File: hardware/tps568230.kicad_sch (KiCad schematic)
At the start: 24 parts, among them U1 TPS568230, U4 LD39050PU33R

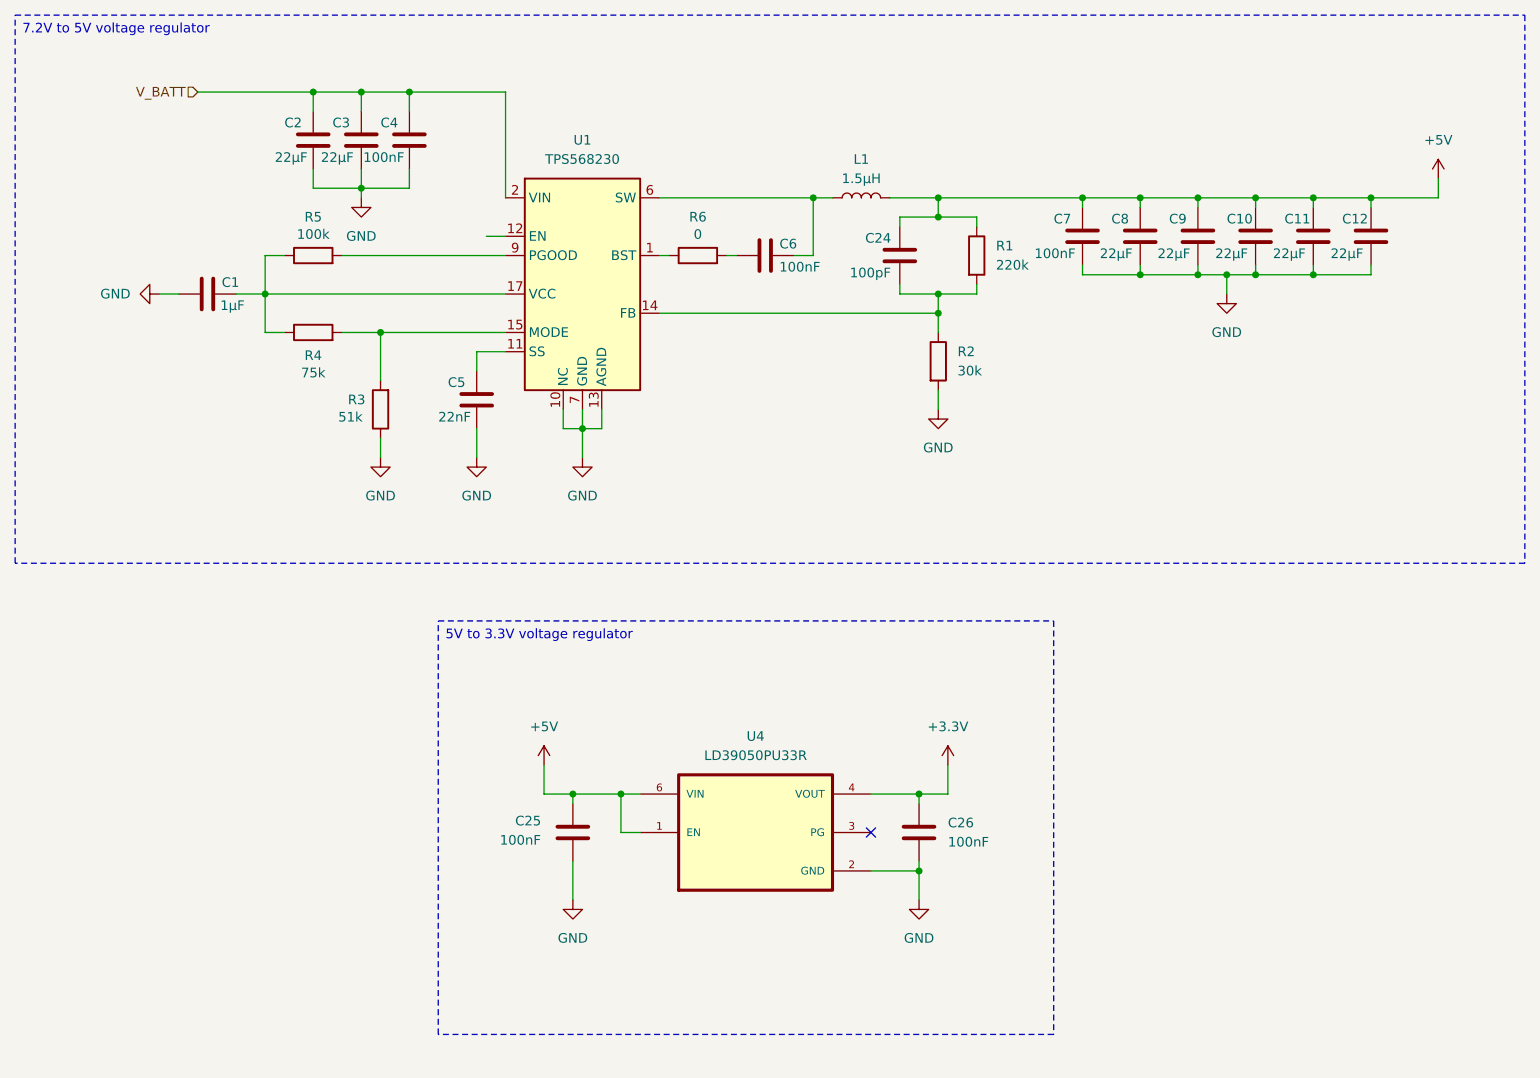
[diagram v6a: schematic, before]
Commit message: Adding voltage divider to EN
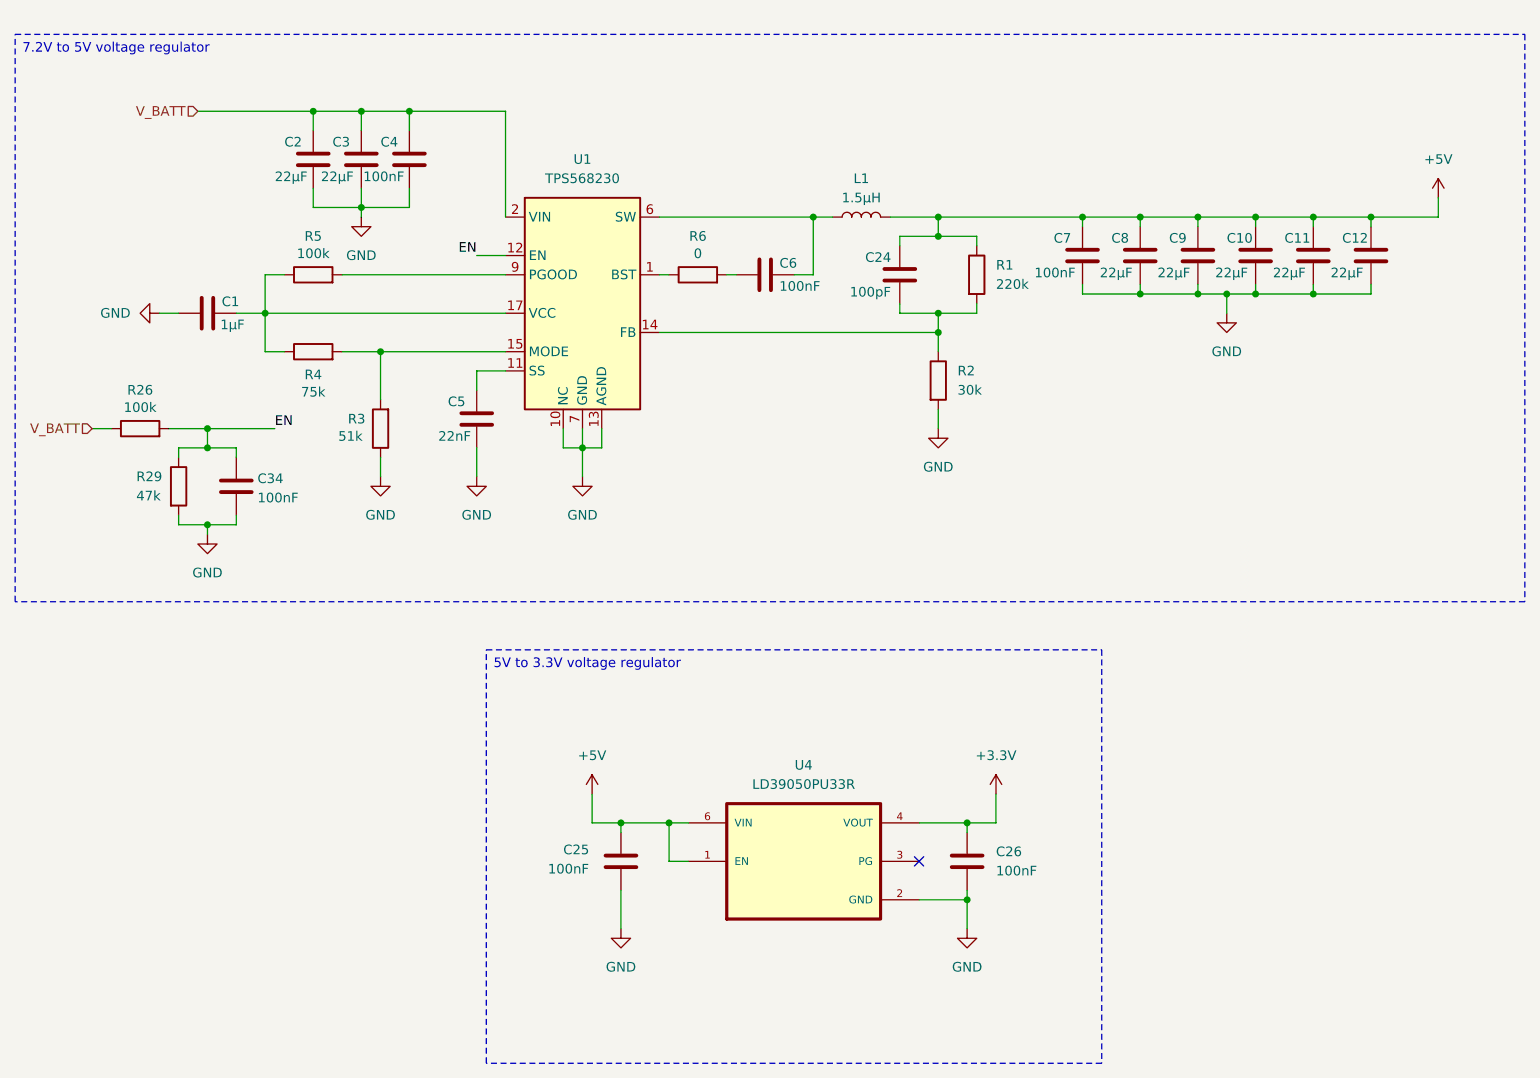
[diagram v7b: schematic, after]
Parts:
- added C34: 100nF, symbol Device:C
- added R26: 100k, symbol Device:R
- added R29: 47k, symbol Device:R
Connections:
- net GND: now also C34.2, R29.2
- net V_BATT: now also R26.1
- net EN: now reaches U1.12 (EN)
- net EN: now also C34.1, R26.2, R29.1
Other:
- moved on the sheet: C1, C10, C11, C12, C2, C24, C25, C26, C3, C4, C5, C6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
